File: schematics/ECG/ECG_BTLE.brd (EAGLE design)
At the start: 25.4 x 25.4 mm, 22 parts, among them IC1 ADS1293, IC3 MCP1703, X1 53261-03

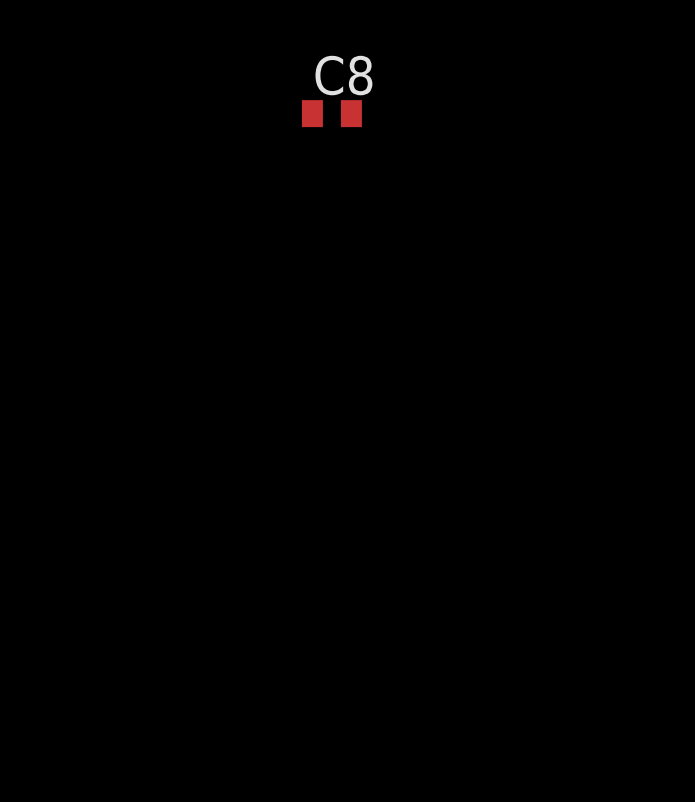
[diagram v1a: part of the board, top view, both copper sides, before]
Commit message: adding individual BLE components instead of module for space saving purposes
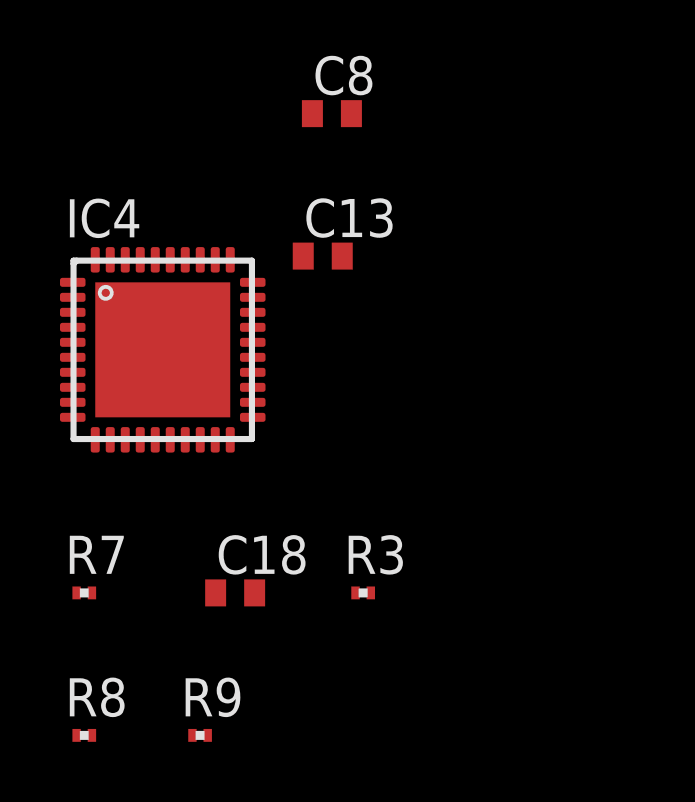
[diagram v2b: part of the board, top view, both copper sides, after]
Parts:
- added C13: 1.0uF, rcl:C0402
- added C18: 1nF, rcl:C0402
- added IC4: CC2541, ST-CC254X:RHA_S-PVQFN-N40
- added R3: 56K, rcl:R0201
- added R7: 2.7K, rcl:R0201
- added R8, R9: 10k, rcl:R0201
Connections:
- new net 16XCLK: IC4.7
- new net DCOUPL1: C13.1, IC4.40
- new net GATE_R: IC4.14
- new net GATE_T: IC4.15
- new net I2C_SCL: IC4.2, R8.1
- new net I2C_SDA: IC4.3, R9.1
- new net IR_SD: IC4.19
- new net MCP_RST: IC4.18
- new net MCU_UART_RX: IC4.17
- new net MCU_UART_TX: IC4.16
- new net N$8: C18.1, IC4.20, R7.1
- new net P0_6: IC4.13
- new net P0_7: IC4.12
- new net P1_1: IC4.9
- new net P1_2/DCDC: IC4.8
- new net P1_4: IC4.6
- new net P1_5: IC4.5
- new net P1_6: IC4.38
- new net P1_7: IC4.37
- new net P2_0: IC4.36
- new net P2_1/DD: IC4.35
- new net P2_2/DC: IC4.34
- new net P2_3/32K_Q2: IC4.33
- new net P2_4/32K_Q1: IC4.32
- new net RESET_N: R7.2
- new net RF_N: IC4.26
- new net RF_P: IC4.25
- new net R_BIAS: IC4.30, R3.1
- new net VCC: IC4.10, IC4.21, IC4.24, IC4.27, IC4.28, IC4.29, IC4.31, IC4.39, R8.2, R9.2
- new net VCC_CONTROL: IC4.11
- new net XOSC_Q1: IC4.23
- new net XOSC_Q2: IC4.22
- net GND: now also C13.2, C18.2, IC4.1, IC4.4, IC4.GND, R3.2
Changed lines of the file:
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@@
 <element name="C7" library="rcl" package="C0402" value="0.1uF" x="-10.7188" y="-30.1498"/>
 <element name="C8" library="rcl" package="C0402" value="0.1uF" x="-10.7188" y="-34.8996"/>
+<element name="R3" library="rcl" package="R0201" value="56K" x="-9.6774" y="-50.8762"/>
+<element name="C13" library="rcl" package="C0402" value="1.0uF" x="-11.0236" y="-39.6494"/>
+<element name="R7" library="rcl" package="R0201" value="2.7K" x="-18.9738" y="-50.8762"/>
+<element name="C18" library="rcl" package="C0402" value="1nF" x="-13.9446" y="-50.8762"/>
+<element name="IC4" library="ST-CC254X" package="RHA_S-PVQFN-N40" value="CC2541" x="-16.3576" y="-42.7736"/>
+<element name="R8" library="rcl" package="R0201" value="10k" x="-18.9738" y="-55.626"/>
+<element name="R9" library="rcl" package="R0201" value="10k" x="-15.113" y="-55.626"/>
 </elements>
 <signals>
@@
 <contactref element="IC1" pad="27"/>
 <contactref element="IC1" pad="14"/>
+<contactref element="C18" pad="2"/>
+<contactref element="R3" pad="2"/>
+<contactref element="C13" pad="2"/>
+<contactref element="IC4" pad="GND"/>
+<contactref element="IC4" pad="1"/>
+<contactref element="IC4" pad="4"/>
+<wire x1="-9.4224" y1="-50.8762" x2="-13.2946" y2="-50.8762" width="0" layer="19" extent="1-1"/>
+<wire x1="-16.3576" y1="-42.7736" x2="-13.2946" y2="-50.8762" width="0" layer="19" extent="1-1"/>
+<wire x1="-19.3576" y1="-42.0236" x2="-16.3576" y2="-42.7736" width="0" layer="19" extent="1-1"/>
+<wire x1="-19.3576" y1="-40.5236" x2="-19.3576" y2="-42.0236" width="0" layer="19" extent="1-1"/>
+<wire x1="-10.3736" y1="-39.6494" x2="-16.3576" y2="-42.7736" width="0" layer="19" extent="1-1"/>
+<wire x1="-10.0688" y1="-34.8996" x2="-10.3736" y2="-39.6494" width="0" layer="19" extent="1-1"/>
 <wire x1="-10.0688" y1="-30.1498" x2="-10.0688" y2="-34.8996" width="0" layer="19" extent="1-1"/>
 <wire x1="1.52" y1="-25.4" x2="-10.0688" y2="-30.1498" width="0" layer="19" extent="1-1"/>
@@
 <wire x1="10.771" y1="15.6842" x2="7.771" y2="15.6842" width="0" layer="19" extent="1-1"/>
 </signal>
+<signal name="VCC">
+<contactref element="IC4" pad="28"/>
+<contactref element="IC4" pad="31"/>
+<contactref element="IC4" pad="21"/>
+<contactref element="IC4" pad="29"/>
+<contactref element="IC4" pad="24"/>
+<contactref element="IC4" pad="27"/>
+<contactref element="IC4" pad="10"/>
+<contactref element="IC4" pad="39"/>
+<contactref element="R8" pad="2"/>
+<contactref element="R9" pad="2"/>
+<wire x1="-14.858" y1="-55.626" x2="-18.7188" y2="-55.626" width="0" layer="19" extent="1-1"/>
+<wire x1="-19.3576" y1="-45.0236" x2="-18.7188" y2="-55.626" width="0" layer="19" extent="1-1"/>
+<wire x1="-18.1076" y1="-39.7736" x2="-19.3576" y2="-45.0236" width="0" layer="19" extent="1-1"/>
+<wire x1="-14.1076" y1="-39.7736" x2="-18.1076" y2="-39.7736" width="0" layer="19" extent="1-1"/>
+<wire x1="-13.3576" y1="-41.0236" x2="-14.1076" y2="-39.7736" width="0" layer="19" extent="1-1"/>
+<wire x1="-13.3576" y1="-41.5236" x2="-13.3576" y2="-41.0236" width="0" layer="19" extent="1-1"/>
+<wire x1="-13.3576" y1="-42.0236" x2="-13.3576" y2="-41.5236" width="0" layer="19" extent="1-1"/>
+<wire x1="-13.3576" y1="-43.5236" x2="-13.3576" y2="-42.0236" width="0" layer="19" extent="1-1"/>
+<wire x1="-13.3576" y1="-45.0236" x2="-13.3576" y2="-43.5236" width="0" layer="19" extent="1-1"/>
+</signal>
+<signal name="RESET_N">
+<contactref element="R7" pad="2"/>
+</signal>
+<signal name="P2_2/DC">
+<contactref element="IC4" pad="34"/>
+</signal>
+<signal name="P2_1/DD">
+<contactref element="IC4" pad="35"/>
+</signal>
+<signal name="P2_3/32K_Q2">
+<contactref element="IC4" pad="33"/>
+</signal>
+<signal name="P2_4/32K_Q1">
+<contactref element="IC4" pad="32"/>
+</signal>
+<signal name="XOSC_Q1">
+<contactref element="IC4" pad="23"/>
+</signal>
+<signal name="XOSC_Q2">
+<contactref element="IC4" pad="22"/>
+</signal>
+<signal name="MCU_UART_TX">
+<contactref element="IC4" pad="16"/>
+</signal>
+<signal name="MCU_UART_RX">
+<contactref element="IC4" pad="17"/>
+</signal>
+<signal name="N$8">
+<contactref element="C18" pad="1"/>
+<contactref element="R7" pad="1"/>
+<contactref element="IC4" pad="20"/>
+<wire x1="-14.5946" y1="-50.8762" x2="-19.2288" y2="-50.8762" width="0" layer="19" extent="1-1"/>
+<wire x1="-14.1076" y1="-45.7736" x2="-14.5946" y2="-50.8762" width="0" layer="19" extent="1-1"/>
+</signal>
+<signal name="R_BIAS">
+<contactref element="IC4" pad="30"/>
+<contactref element="R3" pad="1"/>
+<wire x1="-13.3576" y1="-40.5236" x2="-9.9324" y2="-50.8762" width="0" layer="19" extent="1-1"/>
+</signal>
+<signal name="DCOUPL1">
+<contactref element="IC4" pad="40"/>
+<contactref element="C13" pad="1"/>
+<wire x1="-11.6736" y1="-39.6494" x2="-18.6076" y2="-39.7736" width="0" layer="19" extent="1-1"/>
+</signal>
+<signal name="RF_N">
+<contactref element="IC4" pad="26"/>
+</signal>
+<signal name="RF_P">
+<contactref element="IC4" pad="25"/>
+</signal>
+<signal name="VCC_CONTROL">
+<contactref element="IC4" pad="11"/>
+</signal>
+<signal name="P1_2/DCDC">
+<contactref element="IC4" pad="8"/>
+</signal>
+<signal name="GATE_T">
+<contactref element="IC4" pad="15"/>
+</signal>
+<signal name="GATE_R">
+<contactref element="IC4" pad="14"/>
+</signal>
+<signal name="P1_7">
+<contactref element="IC4" pad="37"/>
+</signal>
+<signal name="I2C_SCL">
+<contactref element="IC4" pad="2"/>
+<contactref element="R8" pad="1"/>
+<wire x1="-19.3576" y1="-41.0236" x2="-19.2288" y2="-55.626" width="0" layer="19" extent="1-1"/>
+</signal>
+<signal name="I2C_SDA">
+<contactref element="IC4" pad="3"/>
+<contactref element="R9" pad="1"/>
+<wire x1="-19.3576" y1="-41.5236" x2="-15.368" y2="-55.626" width="0" layer="19" extent="1-1"/>
+</signal>
+<signal name="P1_6">
+<contactref element="IC4" pad="38"/>
+</signal>
+<signal name="P1_1">
+<contactref element="IC4" pad="9"/>
+</signal>
+<signal name="16XCLK">
+<contactref element="IC4" pad="7"/>
+</signal>
+<signal name="P2_0">
+<contactref element="IC4" pad="36"/>
+</signal>
+<signal name="P1_4">
+<contactref element="IC4" pad="6"/>
+</signal>
+<signal name="P1_5">
+<contactref element="IC4" pad="5"/>
+</signal>
+<signal name="MCP_RST">
+<contactref element="IC4" pad="18"/>
+</signal>
+<signal name="IR_SD">
+<contactref element="IC4" pad="19"/>
+</signal>
+<signal name="P0_7">
+<contactref element="IC4" pad="12"/>
+</signal>
+<signal name="P0_6">
+<contactref element="IC4" pad="13"/>
+</signal>
 </signals>

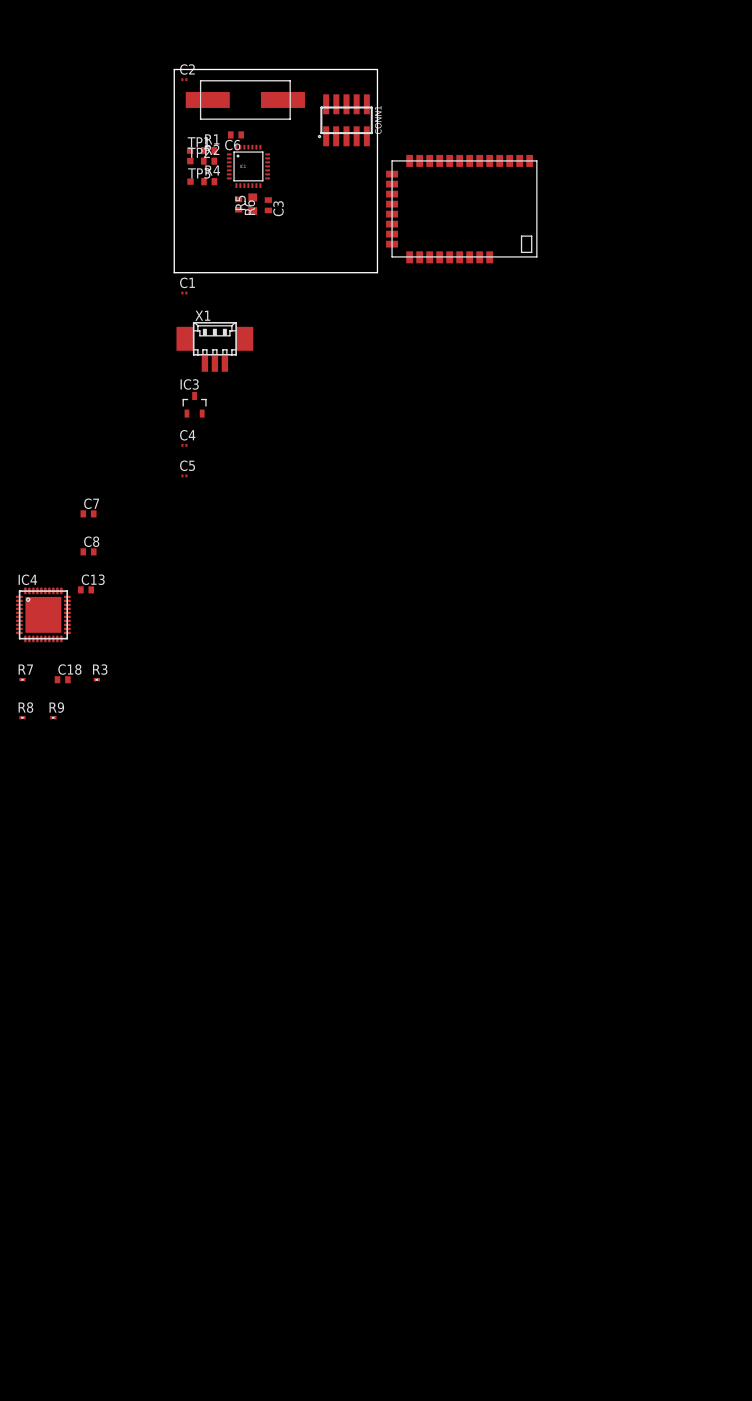
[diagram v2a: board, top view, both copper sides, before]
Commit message: added board to board connectors, removed BLE module
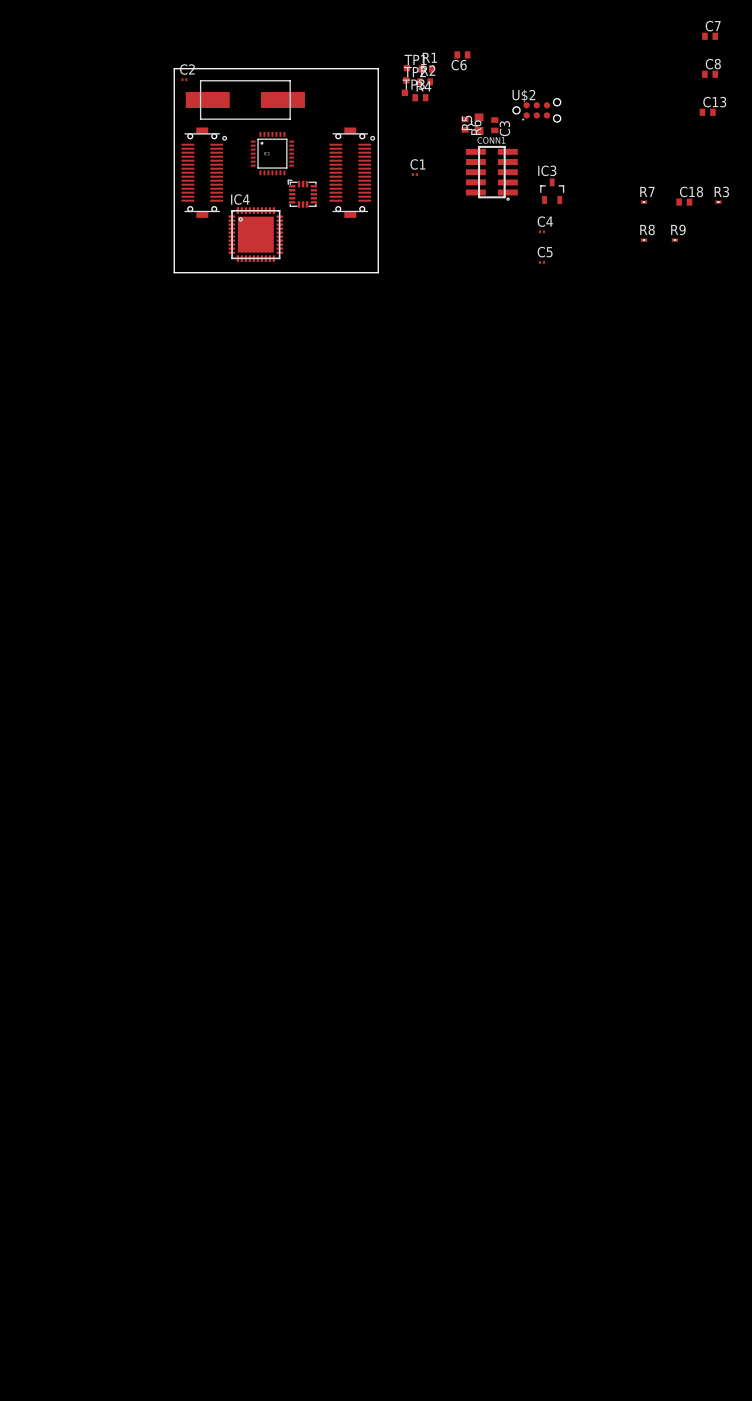
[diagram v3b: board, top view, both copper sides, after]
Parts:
- removed IC2: (no value), bluegiga:BLE112
- removed X1: 53261-03, con-molex:53261-03
- added U$2: TC2030-MCP-NL, tagconnect:TC2030-MCP-NL
- added U$3, U$4: DF12-3.5-30DP, hirose:DF12-3.5-30DP
- added U1: ADXL362, SparkFun-Sensors:ADXL362
- moved C13 98.0 mm to (66.7, 20.1)
- moved C18 98.0 mm to (63.8, 8.82)
- moved C7 98.0 mm to (67.0, 29.6)
- moved C8 98.0 mm to (67.0, 24.8)
- moved R3 98.0 mm to (68.0, 8.82)
- moved R7 98.0 mm to (58.7, 8.82)
- moved R8 98.0 mm to (58.7, 4.07)
- moved R9 98.0 mm to (62.6, 4.07)
- moved IC4 54.4 mm to (10.2, 4.76)
- moved IC3 52.1 mm to (47.2, 10.2)
- moved C4 52.1 mm to (46.0, 5.11)
- moved C5 52.1 mm to (46.0, 1.30)
- moved C1 32.4 mm to (30.1, 12.3)
- moved C3 30.0 mm to (40.1, 18.4)
- moved C6 30.0 mm to (36.0, 27.2)
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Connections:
- new net 2: U$2.2
- new net 3: U$2.3
- net BATT+: no longer X1.3
- net GND: no longer X1.2
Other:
- board size 25.4 x 25.4 mm -> 25.5 x 25.5 mm

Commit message: few changes
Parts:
- added U$5: MICROSD_SD_MODE, con-molex-microsd:MICRO_SD_CONNECTOR
- moved U$1 51.2 mm to (58.9, 10.6)
- moved C2 49.8 mm to (50.3, 15.1)
- moved IC1 36.7 mm to (48.3, 7.88)
- moved IC4 34.1 mm to (44.2, 6.76)
- moved U1 25.5 mm to (41.1, 4.80)
- moved U$4 2.83 mm to (24.0, 14.5)
- moved U$3 2.00 mm to (3.50, 14.5)
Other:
- board size 25.5 x 25.5 mm -> 30 x 30 mm

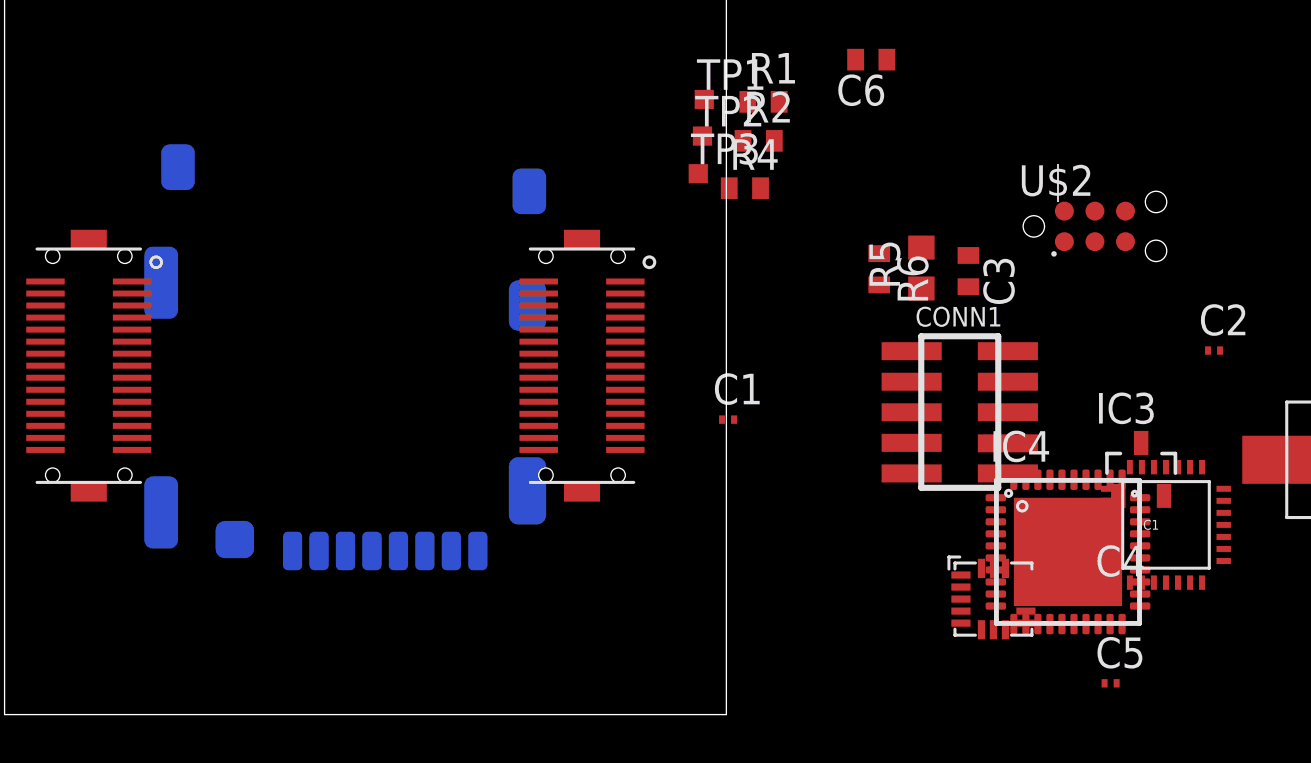
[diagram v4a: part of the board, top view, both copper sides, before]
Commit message: removed some unused parts
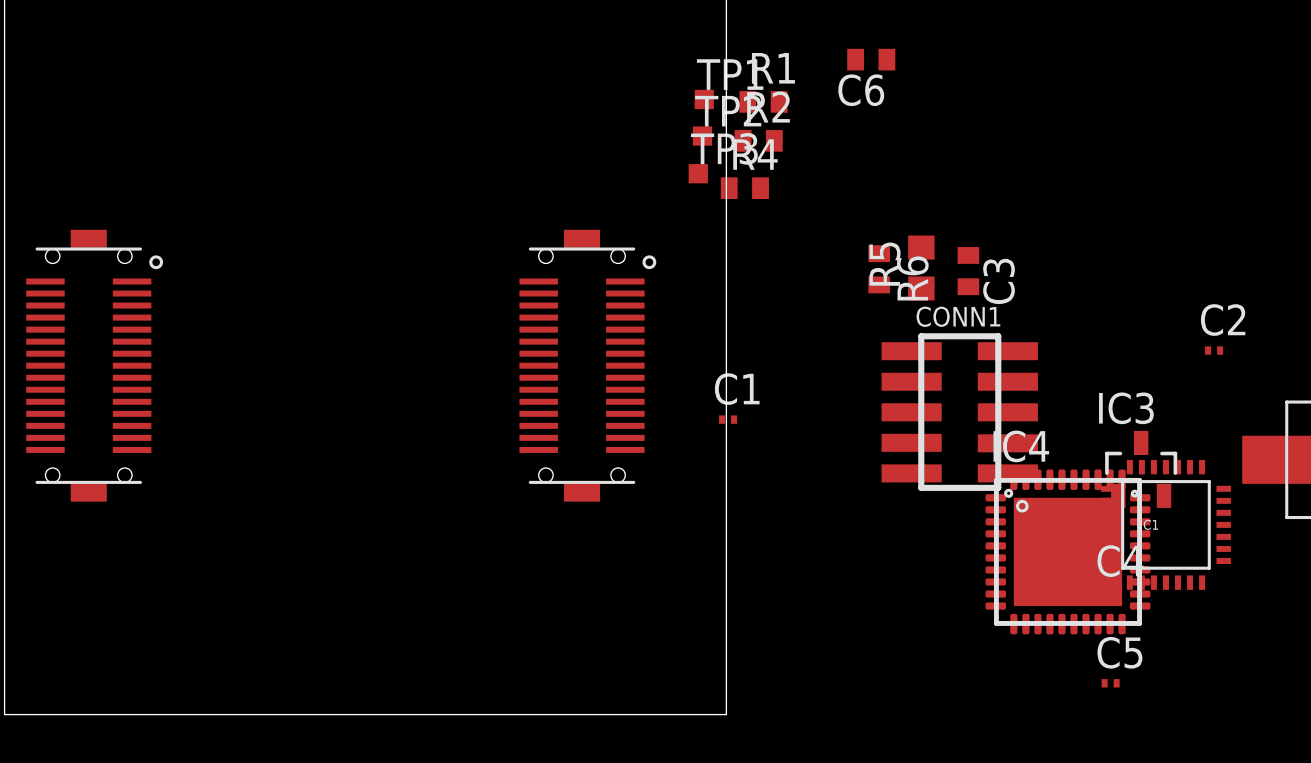
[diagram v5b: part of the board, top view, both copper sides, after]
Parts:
- removed U$2: TC2030-MCP-NL, tagconnect:TC2030-MCP-NL
- removed U$5: MICROSD_SD_MODE, con-molex-microsd:MICRO_SD_CONNECTOR
- removed U1: ADXL362, SparkFun-Sensors:ADXL362
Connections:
- removed net 2: U$2.2
- removed net 3: U$2.3
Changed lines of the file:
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@@
 <element name="R8" library="rcl" package="R0201" value="10k" x="58.7262" y="4.074"/>
 <element name="R9" library="rcl" package="R0201" value="10k" x="62.587" y="4.074"/>
-<element name="U1" library="SparkFun-Sensors" package="ADXL362" value="ADXL362" x="41.1" y="4.8">
-<attribute name="PROD_ID" value="IC-11297" x="41.1" y="4.8" size="1.778" layer="27" display="off"/>
-</element>
-<element name="U$2" library="tagconnect" package="TC2030-MCP-NL" value="TC2030-MCP-NL" x="42.7786" y="20.2902"/>
 <element name="U$3" library="hirose" package="DF12-3.5-30DP" value="DF12-3.5-30DP" x="3.5" y="14.5"/>
 <element name="U$4" library="hirose" package="DF12-3.5-30DP" value="DF12-3.5-30DP" x="24" y="14.5"/>
-<element name="U$5" library="con-molex-microsd" package="MICRO_SD_CONNECTOR" value="MICROSD_SD_MODE" x="14" y="15" rot="MR180"/>
 </elements>
 <signals>
@@
 <contactref element="IC4" pad="13"/>
 </signal>
-<signal name="2">
-<contactref element="U$2" pad="2"/>
-</signal>
-<signal name="3">
-<contactref element="U$2" pad="3"/>
-</signal>
 </signals>
